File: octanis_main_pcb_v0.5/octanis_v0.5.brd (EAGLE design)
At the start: 80 x 48 mm, 103 parts, among them IC1 BME280, IC2 BNO055A, Q1 32.768kHz, Q2 32.768kHz, U1 MSP432, U10 INA213, U11 INA213, U12 MAX6001SOT-23, U2 TPS61232, U3 DRV8836DSSR, U4 DRV8836DSSR, U5 DRV8836DSSR, U6 DRV8836DSSR, U7 SST25VF064C, U8 INA213, U9 INA213

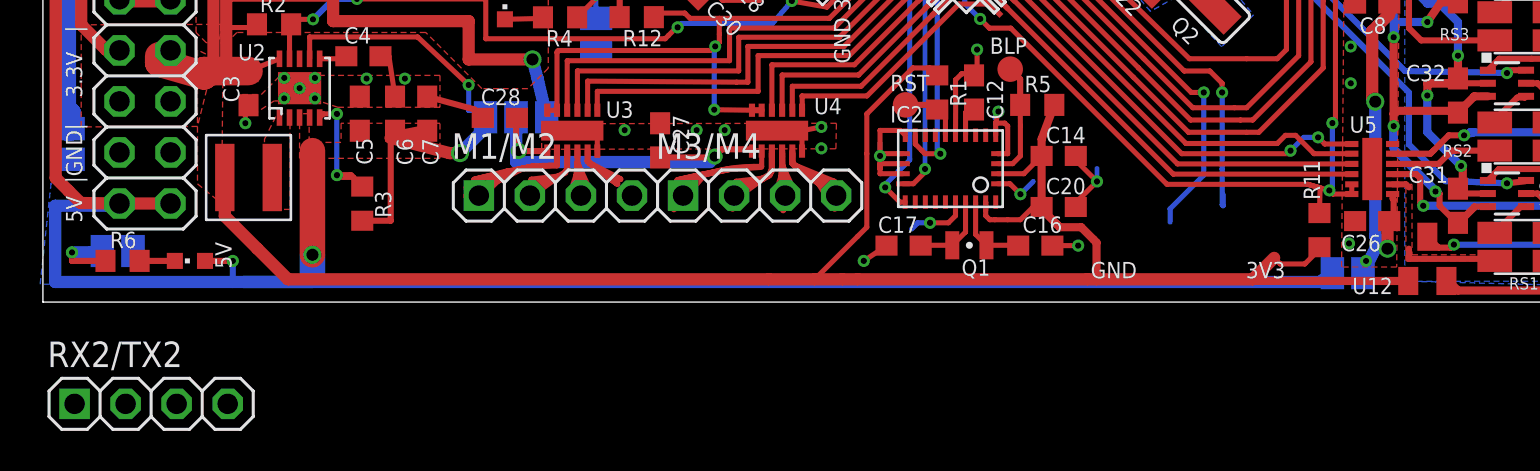
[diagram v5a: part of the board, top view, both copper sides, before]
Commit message: finished revised weather strip
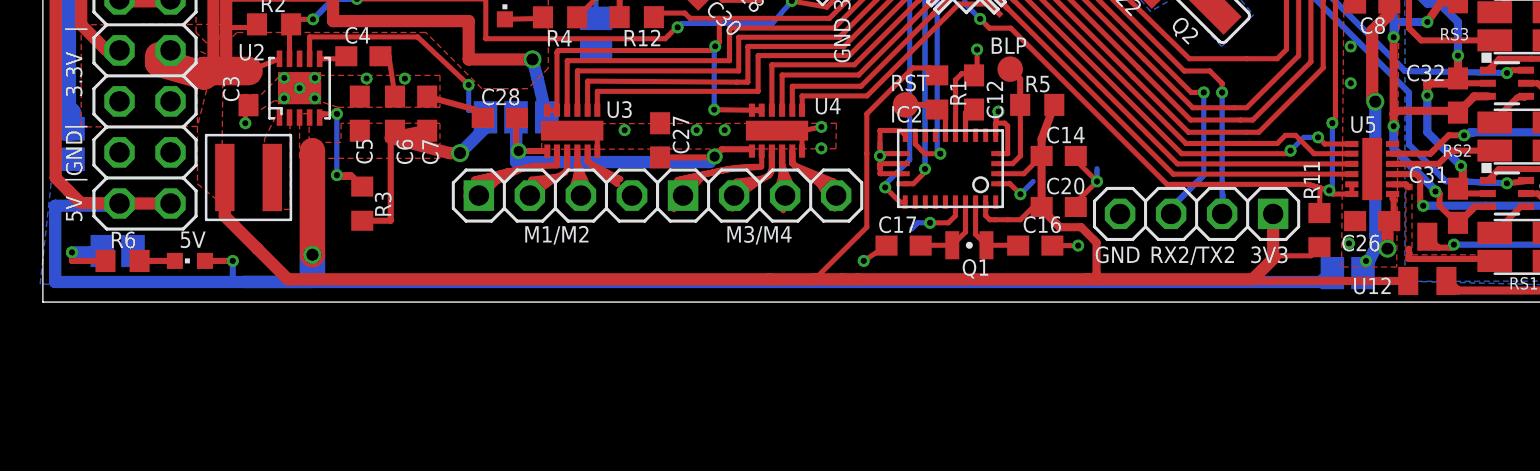
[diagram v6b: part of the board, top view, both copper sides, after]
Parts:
- moved RX2/TX2 52.9 mm to (57.4, 5.38), turned to 180 degrees
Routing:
- net +3V3: track 383.1 -> 385.0 mm
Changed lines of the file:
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@@
 <layers>
 <layer number="1" name="Top" color="4" fill="1" visible="yes" active="yes"/>
-<layer number="16" name="Bottom" color="1" fill="1" visible="no" active="yes"/>
+<layer number="16" name="Bottom" color="1" fill="1" visible="yes" active="yes"/>
 <layer number="17" name="Pads" color="2" fill="1" visible="yes" active="yes"/>
 <layer number="18" name="Vias" color="2" fill="1" visible="yes" active="yes"/>
@@
 <text x="71.0692" y="30.67" size="0.8128" layer="25" rot="R315">A16 A17</text>
 <text x="70.0908" y="29.3624" size="0.8128" layer="25" rot="R315">A18 AGND</text>
-<text x="52.133" y="2.1844" size="0.8128" layer="25">GND                 3V3</text>
+<text x="52.324" y="2.9464" size="0.8128" layer="25">GND                 3V3</text>
 </plain>
 <attributes>
@@
 </element>
 <element name="5V" library="adafruit" package="CHIPLED_0603" value="5V-ok" x="7.3152" y="3.048" smashed="yes" rot="R90">
-<attribute name="NAME" x="8.57555" y="3.98755" size="0.8128" layer="25" rot="R270"/>
+<attribute name="NAME" x="6.78205" y="3.69875" size="0.8128" layer="25"/>
 <attribute name="VALUE" x="8.8646" y="4.3942" size="0.8128" layer="27" rot="R180"/>
 </element>
@@
 <attribute name="VALUE" x="65.2018" y="26.289" size="1.27" layer="27" rot="R180"/>
 </element>
-<element name="M3/M4" library="pinhead-2" package="1X04-S" value="" x="35.6616" y="6.2992"/>
-<element name="M1/M2" library="pinhead-2" package="1X04-S" value="" x="25.5016" y="6.2992"/>
-<element name="RX2/TX2" library="pinhead-2" package="1X04-S" value="" x="5.3848" y="-4.064"/>
+<element name="M3/M4" library="pinhead-2" package="1X04-S" value="" x="35.6616" y="6.2992" smashed="yes">
+<attribute name="NAME" x="33.9598" y="3.9624" size="0.8128" layer="25" ratio="10"/>
+<attribute name="VALUE" x="30.5816" y="3.1242" size="1.27" layer="27"/>
+</element>
+<element name="M1/M2" library="pinhead-2" package="1X04-S" value="" x="25.5016" y="6.2992" smashed="yes">
+<attribute name="NAME" x="23.9014" y="3.9624" size="0.8128" layer="25" ratio="10"/>
+<attribute name="VALUE" x="20.4216" y="3.1242" size="1.27" layer="27"/>
+</element>
+<element name="RX2/TX2" library="pinhead-2" package="1X04-S" value="" x="57.404" y="5.3848" smashed="yes" rot="R180">
+<attribute name="NAME" x="55.0672" y="2.9464" size="0.8128" layer="25" ratio="10"/>
+<attribute name="VALUE" x="62.484" y="8.5598" size="1.27" layer="27" rot="R180"/>
+</element>
 </elements>
 <signals>
@@
 <wire x1="16.5114" y1="20.0646" x2="16.5114" y2="20.6798" width="0.8128" layer="16"/>
 <contactref element="RX2/TX2" pad="4"/>
-<wire x1="4.4788" y1="3.54" x2="9.1948" y2="-4.064" width="0" layer="19" extent="16-16"/>
 </signal>
 <signal name="N$9">
@@
 <wire x1="38.4048" y1="2.1336" x2="36.1188" y2="2.1336" width="0.6096" layer="1"/>
 <wire x1="63.5164" y1="3.7288" x2="63.5164" y2="3.6232" width="0.254" layer="1"/>
-<wire x1="63.5164" y1="3.6232" x2="62.7888" y2="2.8956" width="0.254" layer="1"/>
-<wire x1="62.7888" y1="2.8956" x2="61.5696" y2="2.8956" width="0.254" layer="1"/>
-<wire x1="61.5696" y1="2.8956" x2="61.2648" y2="3.2004" width="0.254" layer="1"/>
+<wire x1="63.5164" y1="3.6232" x2="63.0936" y2="3.302" width="0.254" layer="1"/>
+<wire x1="63.0936" y1="3.302" x2="61.5696" y2="3.302" width="0.254" layer="1"/>
+<wire x1="61.5696" y1="3.302" x2="61.2648" y2="3.2004" width="0.254" layer="1"/>
 <wire x1="44.5008" y1="12.28" x2="44.1316" y2="12.6492" width="0.254" layer="1"/>
 <wire x1="44.1316" y1="12.6492" x2="43.2816" y2="12.6492" width="0.254" layer="1"/>
@@
 <wire x1="40.5384" y1="4.2672" x2="38.4048" y2="2.1336" width="0.254" layer="1"/>
 <contactref element="RX2/TX2" pad="1"/>
-<wire x1="10.668" y1="3.6576" x2="1.5748" y2="-4.064" width="0" layer="19" extent="1-1"/>
+<wire x1="61.2648" y1="3.2004" x2="61.214" y2="3.2512" width="0.6096" layer="1"/>
+<wire x1="61.214" y1="3.2512" x2="61.214" y2="5.3848" width="0.6096" layer="1"/>
 </signal>
 <signal name="M1IN2">
@@
 <wire x1="58.674" y1="11.8872" x2="58.674" y2="11.43" width="0.254" layer="1"/>
 <contactref element="RX2/TX2" pad="2"/>
-<wire x1="4.1148" y1="-4.064" x2="50.27848125" y2="19.007175" width="0" layer="19" extent="1-1"/>
+<wire x1="58.7248" y1="5.7912" x2="58.674" y2="5.7404" width="0.3048" layer="16"/>
+<wire x1="58.674" y1="5.7404" x2="58.674" y2="5.3848" width="0.3048" layer="16"/>
 </signal>
 <signal name="RX2">
@@
 <via x="57.7596" y="11.43" extent="1-16" drill="0.3048"/>
 <wire x1="57.7596" y1="11.43" x2="57.7596" y2="7.3152" width="0.254" layer="16"/>
-<wire x1="57.7596" y1="7.3152" x2="56.0832" y2="5.6388" width="0.254" layer="16"/>
-<wire x1="56.0832" y1="5.6388" x2="56.0832" y2="4.9784" width="0.254" layer="16"/>
 <contactref element="RX2/TX2" pad="3"/>
-<wire x1="6.6548" y1="-4.064" x2="49.919271875" y2="18.647965625" width="0" layer="19" extent="1-1"/>
+<wire x1="57.7596" y1="7.3152" x2="56.134" y2="5.6896" width="0.3048" layer="16"/>
+<wire x1="56.134" y1="5.6896" x2="56.134" y2="5.3848" width="0.3048" layer="16"/>
 </signal>
 <signal name="RX0">

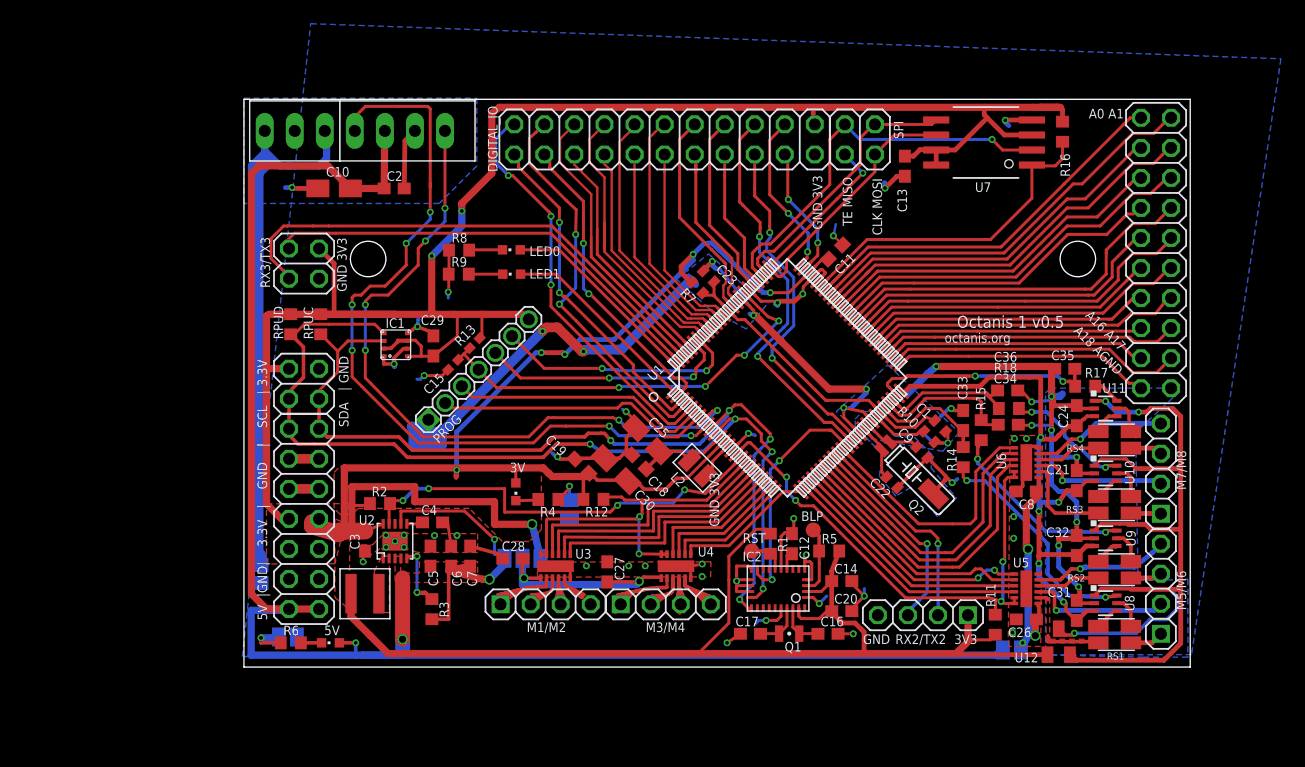
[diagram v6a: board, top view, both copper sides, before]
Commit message: renumbered parts in mainboard
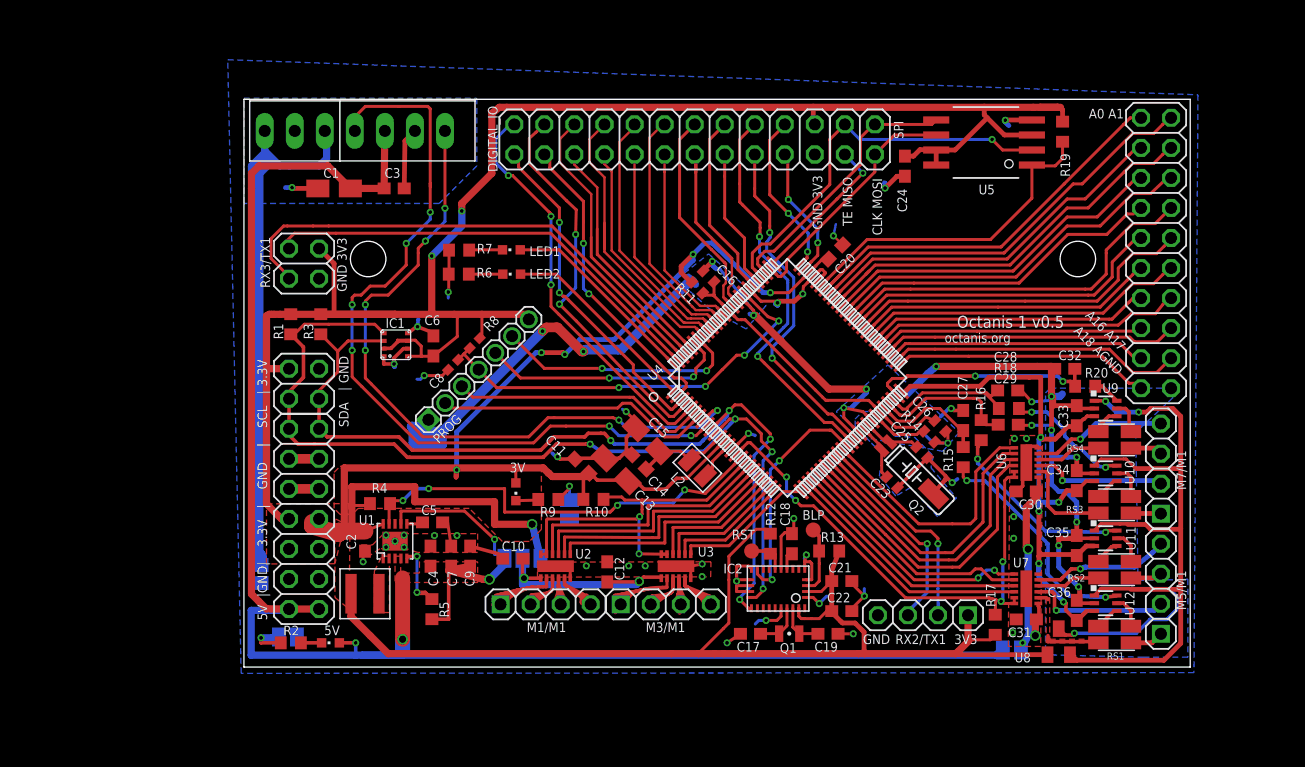
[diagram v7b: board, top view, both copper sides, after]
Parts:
- removed LED0: LED0, adafruit:CHIPLED_0603
- removed RPUC, RPUD: 4.7k, rcl:R0603
- added LED2: LED1, adafruit:CHIPLED_0603
- added R19: 10k, rcl:R0603
- added R20: 6.8k, rcl:R0603
- C1: value 100n -> 10u; device rcl:C0402 -> rcl:A/3216-18R
- C10, C30: value 10u -> 470n; device rcl:A/3216-18R -> rcl:C0603
- C12, C29: value 100n -> 470n
- C13: value 100n -> 10u; device rcl:C0603 -> rcl:A/3216-18R
- C15: value 1n -> 10u; device rcl:0402 -> rcl:A/3216-18R
- C16: value 12p -> 100n; device rcl:C0603 -> rcl:C0402
- C19, C23: value 100n -> 12p
- C2: value 100n -> 22uF
- C20: value 120n -> 100n
- C21, C24: value 10n -> 100n
- C22: value 12p -> 120n; device rcl:C0402 -> rcl:C0603
- C25: value 10u -> 12p; device rcl:A/3216-18R -> rcl:C0402
- C26: value 470n -> 100n; device rcl:C0603 -> rcl:C0402
- C3, C6: value 22uF -> 100n
- C31, C32: value 10n -> 470n
- C33, C34, C35, C36: value 470n -> 10n
- C4: value 10nF -> 22uF
- C5: value 22uF -> 10nF
- C7: value 3 x 22uF -> 22uF
- C8: value 470n -> 1n; device rcl:C0603 -> rcl:0402
- C9: value 12p -> 3 x 22uF; device rcl:C0402 -> rcl:C0603
- LED1: value LED1 -> LED0
- R1: value 10k -> 4.7k
- R10: value 91k 0.1% ±25 ppm/°C -> 10k; device rcl:R0402 -> rcl:R0603
- R11: value 10k -> 0R; device rcl:R0603 -> rcl:R0402
- R13: value 47k -> 10k; device rcl:0402 -> rcl:R0603
- R14: value 6.8k -> 91k 0.1% ±25 ppm/°C; device rcl:R0603 -> rcl:R0402
- R16: value 10k -> 6.8k
- R17: value 6.8k -> 10k
- R2: value 1M -> 1k
- R3: value 1M -> 4.7k
- R4: value 1k -> 1M
- R5: value 10k -> 1M
- R7: value 0R -> 1k; device rcl:R0402 -> rcl:R0603
- R8: value 1k -> 47k; device rcl:R0603 -> rcl:0402
- RS1: value RS1 -> RS4
- RS2: value RS2 -> RS3
- RS3: value RS3 -> RS2
- RS4: value RS4 -> RS1
- U1: value MSP432 -> TPS61232; device MSP-EXP432:PZ100 -> texasinstruments:S-PVSON-N10
- U12: value MAX6001SOT-23 -> INA213; device Octanis1:MAX6001 -> Octanis1_EPS:SC70-6
- U2: value TPS61232 -> DRV8836DSSR; device texasinstruments:S-PVSON-N10 -> DRV8834:SON50P200X300X80-13N
- U4: value DRV8836DSSR -> MSP432; device DRV8834:SON50P200X300X80-13N -> MSP-EXP432:PZ100
- U5: value DRV8836DSSR -> SST25VF064C; device DRV8834:SON50P200X300X80-13N -> BertaLib:SOIC_8-LEAD
- U7: value SST25VF064C -> DRV8836DSSR; device BertaLib:SOIC_8-LEAD -> DRV8834:SON50P200X300X80-13N
- U8: value INA213 -> MAX6001SOT-23; device Octanis1_EPS:SC70-6 -> Octanis1:MAX6001
- moved C1 55.0 mm to (7.62, 41.5), turned to 0 degrees
- moved C8 49.6 mm to (17.7, 26.6), turned to 225 degrees
- moved C29 49.1 mm to (64.6, 21.5), turned to 180 degrees
- moved R1 44.6 mm to (3.95, 30.0), turned to 90 degrees
- moved C28 44.2 mm to (64.6, 24.4), turned to 180 degrees
- moved C9 39.2 mm to (19.1, 10.4), turned to 90 degrees
- moved R11 38.0 mm to (38.3, 33.1), turned to 135 degrees
- moved U5 37.8 mm to (63.7, 45.3), turned to 90 degrees
- moved U7 37.8 mm to (66.1, 7.62), turned to 180 degrees
- moved U1 35.9 mm to (12.8, 11.6), turned to 0 degrees
- moved C13 35.4 mm to (31.5, 17.7), turned to 315 degrees
- moved C10 34.8 mm to (22.7, 10.2)
- moved R13 34.7 mm to (49.5, 10.8), turned to 0 degrees
- moved C30 34.7 mm to (66.1, 15.8), turned to 0 degrees
- moved R6 34.3 mm to (18.2, 34.2)
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- renumbered JP4 to JP2, JP5 to JP1, LED_J1 to LED_J101, LED_J2 to LED_J100, M1/M2 to M1/M1, M3/M4 to M3/M1, M5/M6 to M5/M1, M7/M8 to M7/M1, RX2/TX2 to RX2/TX1, RX3/TX3 to RX3/TX1, U$2 to U$100, U$4 to U$1
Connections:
- net +3V3: now also C13.+, C2.1, C20.2, C21.1, C22.1, C24.1, C6.1, R1.2, R10.2, R12.1, R17.2, R19.2, R3.2, R4.2, R8.2, U1.10, U4.13, U4.73, U5.RST/HOLD, U5.VDD, U5.WP, U8.1; no longer C13.1, C14.1, C19.2, C20.1, C29.1, C3.1, C30.+, R1.1, R12.2, R16.2, R2.2, R5.2, R7.2, RPUC.2, RPUD.2, U1.13, U1.73, U12.1, U2.10, U7.RST/HOLD, U7.VDD, U7.WP
- net +5V: now also C1.+, C3.1, C4.1, C9.1, R5.2, U1.3, U1.4, U1.7; no longer C10.+, C2.1, C5.1, C6.1, R3.2, U2.3, U2.4, U2.7
- net 5VEN: now also R4.1, U1.9, U4.17; no longer R2.1, U1.17, U2.9
- net A0: now also U4.69; no longer U1.69
- net A1: now also U4.68; no longer U1.68
- net A10: now also U4.59; no longer U1.59
- net A11: now also U4.58; no longer U1.58
- net A12: now also U4.57; no longer U1.57
- net A13: now also U4.56; no longer U1.56
- net A14: now also U4.55; no longer U1.55
- net A15: now also U4.54; no longer U1.54
- net A16: now also U4.53; no longer U1.53
- net A17: now also U4.52; no longer U1.52
- net A18: now also U4.51; no longer U1.51
- net A2: now also U4.67; no longer U1.67
- net A20: now also C32.2, R20.1, U4.49; no longer C35.2, R17.1, U1.49
- net A20UNF: now also R20.2, U9.6; no longer R17.2, U11.6
- net A21: now also C28.2, U4.48; no longer C36.2, U1.48
- net A22: now also C29.2, R16.1, U4.47; no longer C34.2, R15.1, U1.47
- net A22UNF: now also R16.2, U11.6; no longer R15.2, U9.6
- net A23: now also C27.2, R15.1, U4.46; no longer C33.2, R14.1, U1.46
- net A23UNF: now also R15.2, U12.6; no longer R14.2, U8.6
- net A3: now also U4.66; no longer U1.66
- net A4: now also U4.65; no longer U1.65
- net A5: now also U4.64; no longer U1.64
- net A6: now also U4.63; no longer U1.63
- net A7: now also U4.62; no longer U1.62
- net A8: now also U4.61; no longer U1.61
- net A9: now also U4.60; no longer U1.60
- net ACCEL_INT: now also U4.37; no longer U1.37
- net ACCEL_N_BOOTLD: now also R13.1; no longer R5.1
- net ACCEL_N_RST: now also R12.2; no longer R1.2
- net AGND: now also C16.2, C26.2, C27.1, C28.1, C29.1, R14.2, U12.2, U4.40, U4.43, U4.84, U8.3; no longer C1.2, C21.1, C23.2, C24.1, C31.1, R10.2, U1.40, U1.43, U1.84, U12.3, U8.2
- net AVCC: now also C16.1, C26.1, R11.1, U4.45, U4.87; no longer C1.1, C23.1, R7.1, U1.45, U1.87
- net CURR_SENSE_EN: now also C33.2, C34.2, C35.2, C36.2, U12.3, U4.50; no longer C21.2, C24.2, C31.2, C32.2, U1.50, U8.3
- net GND: now also C10.1, C13.-, C14.1, C15.-, C19.2, C2.2, C20.1, C21.2, C22.2, C23.1, C24.2, C25.1, C30.1, C31.1, C8.2, C9.2, R6.1, R7.1, U1.EXPAD, U1.GND1, U1.GND2, U1.GND3, U1.GND4, U1.GND5, U2.13, U2.6, U4.15, U4.71, U4.72, U4.82, U5.VSS, U7.13, U7.6; no longer C13.2, C14.2, C15.2, C16.2, C19.1, C20.2, C22.1, C25.-, C26.1, C27.1, C28.1, C29.2, C3.2, C30.-, C8.1, C9.1, R8.1, R9.1, U1.15, U1.71, U1.72, U1.82, U2.EXPAD, U2.GND1, U2.GND2, U2.GND3, U2.GND4, U2.GND5, U4.13, U4.6, U5.13, U5.6, U7.VSS
- net HX1_DATA: now also U4.8; no longer U1.8
- net HX1_EN: now also U4.9; no longer U1.9
- net IND: now also U1.1, U1.2; no longer U2.1, U2.2
- net LED0: now also LED1.A, U4.100; no longer LED0.A, U1.100
- net LED1: now also LED2.A, U4.1; no longer LED1.A, U1.1
- net M1234SLEEP: now also R10.1, U2.11, U2.12, U4.18; no longer R12.1, U1.18, U4.11, U4.12
- net M1IN1: now also U2.10, U4.19; no longer U1.19, U3.10
- net M1IN2: now also U2.9, U4.20; no longer U1.20, U3.9
- net M2IN1: now also U2.8, U4.21; no longer U1.21, U3.8
- net M2IN2: now also U2.7, U4.22; no longer U1.22, U3.7
- net M3IN1: now also U3.10, U4.23; no longer U1.23, U4.10
- net M3IN2: now also U3.9, U4.24; no longer U1.24, U4.9
- net M4IN1: now also U3.8, U4.25; no longer U1.25, U4.8
- net M4IN2: now also U3.7, U4.26; no longer U1.26, U4.7
- net M5678SLEEP: now also R17.1, U4.16, U7.11, U7.12; no longer R11.1, U1.16, U5.11, U5.12
- net M5IN1: now also U4.27, U7.10; no longer U1.27, U5.10
- net M5IN2: now also U4.28, U7.9; no longer U1.28, U5.9
- net M5OUT1: now also RS4.I1, U7.2; no longer RS1.I1, U5.2
- net M6IN1: now also U4.30, U7.8; no longer U1.30, U5.8
- net M6IN2: now also U4.29, U7.7; no longer U1.29, U5.7
- net M7IN1: now also U4.31; no longer U1.31
- net M7IN2: now also U4.32; no longer U1.32
- net M8IN1: now also U4.33; no longer U1.33
- net M8IN2: now also U4.36; no longer U1.36
- net N$1: now also C14.2, C15.+, U4.12; no longer C18.2, C25.+, U1.12
- net N$10: now also C25.2, U4.42; no longer C9.2, U1.42
- net N$13: now also U3.2; no longer U4.2
- net N$14: now also R2.1; no longer R6.1
- net N$15: now also RS4.V2, U12.5; no longer RS1.V2, U8.5
- net N$17: now also RS4.V1, U12.4; no longer RS1.V1, U8.4
- net N$18: now also C18.2; no longer C12.2
- net N$19: now also C19.1; no longer C16.1
- net N$2: now also R5.1, U1.5; no longer R3.1, U2.5
- net N$21: now also RS4.I2; no longer RS1.I2
- net N$23: now also RS3.V1, U11.4; no longer RS2.V1, U9.4
- net N$24: now also RS3.V2, U11.5; no longer RS2.V2, U9.5
- net N$25: now also RS3.I1, U7.4; no longer RS2.I1, U5.4
- net N$26: now also R9.1; no longer R4.1
- net N$27: now also RS3.I2; no longer RS2.I2
- net N$28: now also RS2.V2; no longer RS3.V2
- net N$29: now also RS2.V1; no longer RS3.V1
- net N$30: now also RS1.V2, U9.5; no longer RS4.V2, U11.5
- net N$31: now also RS1.V1, U9.4; no longer RS4.V1, U11.4
- net N$32: now also RS2.I2; no longer RS3.I2
- net N$33: now also R14.1, U4.44; no longer R10.1, U1.44
- net N$34: now also U4.14; no longer U1.14
- net N$35: now also RS1.I1; no longer RS4.I1
- net N$36: now also RS2.I1; no longer RS3.I1
- net N$37: now also RS1.I2; no longer RS4.I2
- net N$38: now also U7.3; no longer U5.3
- net N$39: now also U3.3; no longer U4.3
- net N$4: now also R9.2; no longer R4.2
- net N$40: now also U3.4; no longer U4.4
- net N$41: now also U3.5; no longer U4.5
- net N$42: now also C5.1, U1.6; no longer C4.1, U2.6
- net N$43: now also U7.5; no longer U5.5
- net N$44: now also R2.2; no longer R6.2
- net N$49: now also U2.2; no longer U3.2
- net N$5: now also LED1.C, R7.2; no longer LED0.C, R8.2
- net N$50: now also U2.3; no longer U3.3
- net N$51: now also U2.4; no longer U3.4
- net N$52: now also U2.5; no longer U3.5
- net N$6: now also LED2.C, R6.2; no longer LED1.C, R9.2
- net N$76: now also U4.94; no longer U1.94
- net N$77: now also U4.95; no longer U1.95
- net N$8: now also C23.2, U4.41; no longer C22.2, U1.41
- net P1.0: now also U4.4; no longer U1.4
- net P1.1: now also U4.5; no longer U1.5
- net P10.2: now also U4.2; no longer U1.2
- net P10.3: now also U4.3; no longer U1.3
- net P3.6: now also U4.38; no longer U1.38
- net P3.7: now also U4.39; no longer U1.39
- net P6.6: now also U4.80; no longer U1.80
- net P6.7: now also U4.81; no longer U1.81
- net P7.0: now also U4.88; no longer U1.88
- net P7.1: now also U4.89; no longer U1.89
- net P7.2: now also U4.90; no longer U1.90
- net P7.3: now also U4.91; no longer U1.91
- net P9.2: now also U4.74; no longer U1.74
- net P9.3: now also U4.75; no longer U1.75
- net P9.4: now also U4.96; no longer U1.96
- net P9.5: now also U4.97; no longer U1.97
- net PJ.2: now also U4.85; no longer U1.85
- net PJ.3: now also U4.86; no longer U1.86
- net PJ.4: now also U4.92; no longer U1.92
- net PJ.5: now also U4.93; no longer U1.93
- net RFGND: now also C1.-, C3.2; no longer C10.-, C2.2
- net RST_N: now also C8.1, R8.1, U4.83; no longer C15.1, R13.1, U1.83
- net RX0: now also U4.6; no longer U1.6
- net RX2: now also U4.34; no longer U1.34
- net RX3: now also U4.98; no longer U1.98
- net SCL: now also R1.1, U4.11; no longer RPUD.1, U1.11
- net SDA: now also R3.1, U4.10; no longer RPUC.1, U1.10
- net SPI_EXTSLAVE_TE: now also U4.76; no longer U1.76
- net SPI_FLASH_CS: now also R19.1, U4.70, U5.CE; no longer R16.1, U1.70, U7.CE
- net SPI_MISO: now also U4.79, U5.SO; no longer U1.79, U7.SO
- net SPI_MOSI: now also U4.78, U5.SI; no longer U1.78, U7.SI
- net SPI_SCK: now also U4.77, U5.SCK; no longer U1.77, U7.SCK
- net TX0: now also U4.7; no longer U1.7
- net TX2: now also U4.35; no longer U1.35
- net TX3: now also U4.99; no longer U1.99
- net VREF_M: now also U12.1, U8.2; no longer U12.2, U8.1
- net V_MOTOR: now also C10.2, C12.2, U2.1; no longer C27.2, C28.2, U4.1
- net V_MOTOR2: now also C30.2, C31.2, U7.1; no longer C26.2, C8.2, U5.1
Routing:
- net N$52: track 6.25 -> 8.48 mm
- net N$13: track 4.20 -> 6.05 mm
- net N$49: track 13.2 -> 14.9 mm
- net N$50: track 6.71 -> 7.43 mm
